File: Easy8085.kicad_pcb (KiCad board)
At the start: 2 copper layers, 37 parts, among them J1 5V Power, J2 EXPANSION, J3 FTDI, SW1 RESET, U1 8085, U2 74LS139, U3 74LS573, U4 CY62256, U5 X28256, U6 8251A, U7 74LS90, Y1 6.144M

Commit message: re-working PCB and schematic to seperate expansion connector and reduce parts.
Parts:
- removed R10, R11, R5, R6, R7, R8, R9: 4.7K, Resistor_THT:R_Axial_DIN0204_L3.6mm_D1.6mm_P7.62mm_Horizontal
- added J4: EXPANSION_B, Connector_PinHeader_2.54mm:PinHeader_1x20_P2.54mm_Vertical, F.Cu at (110.5, 85.1)
- added J5: EXPANSION_D, Connector_PinHeader_2.54mm:PinHeader_1x10_P2.54mm_Vertical, F.Cu at (113.0, 85.1)
- added J6: FTDI, Connector_PinSocket_2.54mm:PinSocket_1x06_P2.54mm_Horizontal, F.Cu at (259.1, 29.4)
- added RN1: 10K, Resistor_THT:R_Array_SIP10, F.Cu at (75.6, 113.0)
- J2: value EXPANSION -> EXPANSION_A; footprint Connector_PinHeader_2.54mm:PinHeader_2x25_P2.54mm_Vertical -> Connector_PinHeader_2.54mm:PinHeader_1x20_P2.54mm_Vertical
- J3: value FTDI -> EXPANSION_C; footprint Connector_PinSocket_2.54mm:PinSocket_1x06_P2.54mm_Horizontal -> Connector_PinHeader_2.54mm:PinHeader_1x10_P2.54mm_Vertical
- U1: footprint Package_DIP:DIP-40_W15.24mm -> Package_DIP:DIP-40_W15.24mm_Socket
- U2: footprint Package_DIP:DIP-16_W7.62mm -> Package_DIP:DIP-16_W7.62mm_Socket
- U3: footprint Package_DIP:DIP-20_W7.62mm -> Package_DIP:DIP-20_W7.62mm_Socket
- U4, U6: footprint Package_DIP:DIP-28_W15.24mm -> Package_DIP:DIP-28_W15.24mm_Socket
- U7: footprint Package_DIP:DIP-14_W7.62mm -> Package_DIP:DIP-14_W7.62mm_Socket
- moved C5 192.4 mm to (262.3, 51.4), turned to 0 degrees
- moved C7 170.9 mm to (198.1, 64.8), turned to 0 degrees
- moved C11 158.3 mm to (251.5, 52.1)
- moved C6 156.0 mm to (193.5, 100.9), turned to 0 degrees
- moved SW1 153.0 mm to (219.3, 66.4)
- moved C8 144.5 mm to (247.0, 61.0)
- moved R3 138.1 mm to (208.2, 66.0), turned to 0 degrees
- moved R4 130.8 mm to (194.6, 93.5), turned to 0 degrees
- moved LED1 125.9 mm to (77.5, 146.7), turned to -90 degrees
- moved C9 124.2 mm to (238.8, 53.3), turned to 0 degrees
- moved R1 113.3 mm to (73.7, 137.8), turned to 180 degrees
- moved C12 113.1 mm to (208.3, 83.8)
- moved J1 112.7 mm to (62.9, 141.0), turned to -90 degrees
- moved R2 111.3 mm to (182.9, 100.7), turned to 0 degrees
- moved C1 111.3 mm to (69.8, 141.6)
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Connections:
- J2 pad 10: /S1 -> /~{INTA}
- J2 pad 11: /RST7.5 -> /AD0
- J2 pad 12: /~{RD} -> /AD1
- J2 pad 13: /RST5.5 -> /AD2
- J2 pad 14: /~{WR} -> /AD3
- J2 pad 15: /INTR -> /AD4
- J2 pad 16: /ALE -> /AD5
- J2 pad 17: /~{INTA} -> /AD6
- J2 pad 18: /S0 -> /AD7
- J2 pad 19: /A0 -> GND
- J2 pad 2: /CLK -> /RES_OUT
- J2 pad 20: /AD0 -> GND
- J2 pad 3: /RES_OUT -> /SOD
- J2 pad 4: /~{RES_IN} -> /SID
- J2 pad 5: /SOD -> /TRAP
- J2 pad 6: /READY -> /RST7.5
- J2 pad 7: /SID -> GND
- J2 pad 8: /IO/~{M} -> /RST5.5
- J2 pad 9: /TRAP -> /INTR
- J3 pad 1: GND -> /ALE
- J3 pad 2: /~{RTS} -> /A0
- J3 pad 3: VCC -> /A1
- J3 pad 4: /RxD -> /A2
- J3 pad 5: /TxD -> /A3
- J3 pad 6: /~{CTS} -> /A4
- R4 pad 1: GND -> VCC
- R4 pad 2: /HOLD -> Net-(R4-Pad2)
- U3 pad 12: /A0 -> /A7
- U3 pad 13: /A1 -> /A6
- U3 pad 14: /A2 -> /A5
- U3 pad 15: /A3 -> /A4
- U3 pad 16: /A4 -> /A3
- U3 pad 17: /A5 -> /A2
- U3 pad 18: /A6 -> /A1
- U3 pad 19: /A7 -> /A0
- U3 pad 2: /AD7 -> /AD0
- U3 pad 3: /AD6 -> /AD1
- U3 pad 4: /AD5 -> /AD2
- U3 pad 5: /AD4 -> /AD3
- U3 pad 6: /AD3 -> /AD4
- U3 pad 7: /AD2 -> /AD5
- U3 pad 8: /AD1 -> /AD6
- U3 pad 9: /AD0 -> /AD7
- U5 pad 27: Net-(R11-Pad2) -> Net-(R4-Pad2)
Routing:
- net /IO/~{M}: track 130.4 -> 0.00 mm
- net /READY: track 86.5 -> 0.00 mm, vias 2 -> 0
- net /~{RES_IN}: track 76.1 -> 0.00 mm
- net /ALE: track 71.5 -> 0.00 mm, vias 2 -> 0
- net /S1: track 63.1 -> 0.00 mm
- net /~{WR}: track 61.8 -> 0.00 mm
- net VCC: track 60.9 -> 0.00 mm
- net /~{RD}: track 60.2 -> 0.00 mm
- net /S0: track 53.6 -> 0.00 mm
- net /RST5.5: track 49.4 -> 0.00 mm
- net /RST7.5: track 48.8 -> 0.00 mm
- net /TRAP: track 46.3 -> 0.00 mm
- net /INTR: track 46.2 -> 0.00 mm
- net /SID: track 44.1 -> 0.00 mm
- net /~{INTA}: track 42.4 -> 0.00 mm
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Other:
- board outline added: 99.1 x 99.1 mm
- copper layers 2 -> 4

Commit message: Continuing PCB layout.
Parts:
- moved J6 203.8 mm to (57.2, 57.7)
- moved SW1 123.9 mm to (95.5, 70.6), turned to 90 degrees
- moved R3 114.5 mm to (95.4, 85.3), turned to -90 degrees
- moved R4 86.8 mm to (125.1, 145.4), turned to 90 degrees
- moved R2 83.0 mm to (100.5, 90.4), turned to 90 degrees
- moved D1 61.1 mm to (97.9, 82.8), turned to -90 degrees
- moved J3 58.1 mm to (55.4, 103.1)
- moved C2 15.0 mm to (100.5, 77.0), turned to 180 degrees
- moved RN1 10.1 mm to (73.2, 103.2)
- moved C1 7.75 mm to (76.2, 137.2)
- moved J5 5.14 mm to (111.3, 80.3)
- moved J2 5.14 mm to (57.9, 80.3)
- moved U3 5.14 mm to (61.7, 103.1)
- moved J4 5.14 mm to (108.7, 80.3)
- moved C3 5.14 mm to (82.6, 72.0)
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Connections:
- J3 pad 1: /ALE -> GND
- J3 pad 10: GND -> /ALE
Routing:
- net /HLDA: track 0.00 -> 73.6 mm
- net /~{INTA}: track 0.00 -> 50.4 mm
- net /INTR: track 0.00 -> 45.9 mm
- net /RST5.5: track 0.00 -> 42.0 mm
- net /HOLD: track 0.00 -> 41.5 mm
- net /A15: track 0.00 -> 40.9 mm
- net /S0: track 0.00 -> 37.6 mm
- net /A14: track 0.00 -> 37.1 mm
- net /A13: track 0.00 -> 33.2 mm
- net /RST7.5: track 0.00 -> 32.9 mm
- net /SID: track 0.00 -> 31.8 mm
- net /A12: track 0.00 -> 29.5 mm
- net /TRAP: track 0.00 -> 28.8 mm
- net /~{WR}: track 0.00 -> 28.7 mm
- net /A11: track 0.00 -> 25.5 mm
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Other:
- outline, holes or cut-outs redrawn

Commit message: Still working on layout - what a pain.
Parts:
- U3: moved to B.Cu
- moved U5 201.1 mm to (-51.7, 103.9)
- moved C3 120.1 mm to (-34.3, 44.8)
- moved C4 120.1 mm to (-29.2, 44.8)
- moved D1 120.1 mm to (-19.1, 55.6)
- moved R2 120.1 mm to (-16.5, 63.2)
- moved R3 120.1 mm to (-21.6, 58.2)
- moved RN1 120.1 mm to (-43.8, 76.1)
- moved U1 120.1 mm to (-39.4, 53.1)
- moved Y1 120.1 mm to (-29.3, 48.6)
- moved U4 116.8 mm to (194.1, 26.4), turned to -90 degrees
- moved C1 102.9 mm to (92.7, 35.6)
- moved J1 102.9 mm to (80.3, 34.3)
- moved R1 102.9 mm to (91.4, 31.8)
- moved LED1 102.1 mm to (82.5, 45.7)
- moved U3 93.0 mm to (-27.9, 78.5), turned to 180 degrees
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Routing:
- net /HLDA: track 73.6 -> 0.00 mm
- net /~{INTA}: track 50.4 -> 0.00 mm
- net /AD7: track 20.7 -> 70.0 mm
- net /AD6: track 20.7 -> 66.3 mm
- net /AD5: track 20.7 -> 62.3 mm
- net /A15: track 40.9 -> 0.00 mm
- net /INTR: track 45.9 -> 6.80 mm
- net /S0: track 37.6 -> 0.00 mm
- net /AD4: track 20.7 -> 58.0 mm
- net /A8: track 15.9 -> 52.3 mm
- net /RST5.5: track 42.0 -> 6.80 mm
- net /AD3: track 20.7 -> 54.9 mm
- net /~{WR}: track 28.7 -> 0.00 mm
- net /RST7.5: track 32.9 -> 6.80 mm
- net /A13: track 33.2 -> 59.0 mm
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
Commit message: Changing to 4 layer board.
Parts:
- U3: moved to F.Cu
- moved RN1 156.8 mm to (106.7, 120.0)
- moved C3 155.7 mm to (115.0, 88.8)
- moved C4 155.7 mm to (120.2, 88.8)
- moved D1 155.7 mm to (130.3, 99.6)
- moved R2 155.7 mm to (132.8, 107.2)
- moved R3 155.7 mm to (127.8, 102.1)
- moved U1 155.7 mm to (110.0, 97.0)
- moved Y1 155.7 mm to (120.1, 92.6)
- moved U4 144.9 mm to (77.5, 112.4), turned to 0 degrees
- moved U3 131.5 mm to (95.9, 122.6), turned to 0 degrees
- moved J1 116.2 mm to (82.5, 150.5), turned to 0 degrees
- moved U5 108.6 mm to (56.6, 112.2), turned to 0 degrees
- moved J6 107.3 mm to (113.1, 149.3), turned to 90 degrees
- moved U2 104.2 mm to (78.7, 107.9)
- moved J3 93.2 mm to (128.3, 45.1)
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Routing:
- net /AD7: track 70.0 -> 0.00 mm
- net /AD6: track 66.3 -> 0.00 mm
- net /AD5: track 62.3 -> 0.00 mm
- net /A13: track 59.0 -> 0.00 mm
- net /AD4: track 58.0 -> 0.00 mm
- net /AD3: track 54.9 -> 0.00 mm
- net /A8: track 52.3 -> 0.00 mm
- net /A14: track 43.2 -> 0.00 mm, vias 1 -> 0
- net /AD2: track 38.3 -> 0.00 mm
- net /A12: track 38.3 -> 0.00 mm
- net /AD1: track 32.9 -> 0.00 mm
- net /AD0: track 25.7 -> 0.00 mm
- net /HOLD: track 25.3 -> 0.00 mm
- net /A5: track 17.0 -> 0.00 mm
- net /A3: track 17.0 -> 0.00 mm
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
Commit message: 4 layer board continued...
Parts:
- removed J4: EXPANSION_B, Connector_PinHeader_2.54mm:PinHeader_1x20_P2.54mm_Vertical
- removed J5: EXPANSION_D, Connector_PinHeader_2.54mm:PinHeader_1x10_P2.54mm_Vertical
- removed J6: FTDI, Connector_PinSocket_2.54mm:PinSocket_1x06_P2.54mm_Horizontal
- J2: value EXPANSION_A -> Expansion; footprint Connector_PinHeader_2.54mm:PinHeader_1x20_P2.54mm_Vertical -> Connector_PinHeader_2.54mm:PinHeader_2x25_P2.54mm_Vertical
- J3: value EXPANSION_C -> FTDI; footprint Connector_PinHeader_2.54mm:PinHeader_1x10_P2.54mm_Vertical -> Connector_PinSocket_2.54mm:PinSocket_1x06_P2.54mm_Horizontal
- moved C9 205.5 mm to (63.5, 160.7)
- moved C8 190.8 mm to (78.7, 150.9)
- moved C5 190.4 mm to (98.4, 148.5), turned to 180 degrees
- moved C11 181.4 mm to (75.1, 94.0), turned to -90 degrees
- moved J2 143.4 mm to (81.3, 156.8), turned to 90 degrees
- moved C7 128.2 mm to (75.7, 102.9), turned to -90 degrees
- moved SW1 123.7 mm to (67.4, 83.9), turned to 0 degrees
- moved C2 85.1 mm to (132.1, 93.3)
- moved R1 77.8 mm to (59.7, 102.7), turned to 0 degrees
- moved C12 69.9 mm to (147.1, 117.5), turned to 90 degrees
- moved C6 68.6 mm to (125.2, 94.3), turned to 90 degrees
- moved C1 62.9 mm to (69.2, 93.9)
- moved LED1 62.7 mm to (56.5, 102.7), turned to 180 degrees
- moved J1 62.0 mm to (62.2, 91.9), turned to -90 degrees
- moved R4 61.7 mm to (60.3, 160.7), turned to 180 degrees
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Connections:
- J2 pad 10: /~{INTA} -> /RST7.5
- J2 pad 11: /AD0 -> /IO/~{M}
- J2 pad 12: /AD1 -> /RST5.5
- J2 pad 13: /AD2 -> /~{RD}
- J2 pad 14: /AD3 -> /INTR
- J2 pad 15: /AD4 -> /~{WR}
- J2 pad 16: /AD5 -> /~{INTA}
- J2 pad 17: /AD6 -> /A15
- J2 pad 18: /AD7 -> /AD0
- J2 pad 19: GND -> /A14
- J2 pad 20: GND -> /A0
- J2 pad 3: /SOD -> /HOLD
- J2 pad 4: /SID -> /SOD
- J2 pad 5: /TRAP -> /HLDA
- J2 pad 6: /RST7.5 -> /SID
- J2 pad 7: GND -> /CLK
- J2 pad 8: /RST5.5 -> /TRAP
- J2 pad 9: /INTR -> /~{RES_IN}
- J3 pad 2: /A0 -> /~{RTS}
- J3 pad 3: /A1 -> VCC
- J3 pad 4: /A2 -> /RxD
- J3 pad 5: /A3 -> /TxD
- J3 pad 6: /A4 -> /~{CTS}
- U3 pad 12: /A7 -> /A0
- U3 pad 13: /A6 -> /A1
- U3 pad 14: /A5 -> /A2
- U3 pad 15: /A4 -> /A3
- U3 pad 16: /A3 -> /A4
- U3 pad 17: /A2 -> /A5
- U3 pad 18: /A1 -> /A6
- U3 pad 19: /A0 -> /A7
- U3 pad 2: /AD0 -> /AD7
- U3 pad 3: /AD1 -> /AD6
- U3 pad 4: /AD2 -> /AD5
- U3 pad 5: /AD3 -> /AD4
- U3 pad 6: /AD4 -> /AD3
- U3 pad 7: /AD5 -> /AD2
- U3 pad 8: /AD6 -> /AD1
- U3 pad 9: /AD7 -> /AD0
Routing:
- net /~{RES_IN}: track 0.00 -> 90.3 mm
- net /AD7: track 0.00 -> 83.5 mm
- net /AD6: track 0.00 -> 79.9 mm
- net /AD5: track 0.00 -> 75.6 mm
- net /AD4: track 0.00 -> 72.1 mm
- net /AD3: track 0.00 -> 68.7 mm
- net /A12: track 0.00 -> 64.9 mm
- net /A1: track 0.00 -> 44.7 mm, vias 0 -> 1
- net /A0: track 0.00 -> 40.9 mm, vias 0 -> 1
- net /ALE: track 0.00 -> 30.3 mm
- net /AD2: track 0.00 -> 29.9 mm
- net /A6: track 0.00 -> 26.0 mm
- net /A7: track 0.00 -> 25.8 mm
- net /AD1: track 0.00 -> 24.4 mm
- net /A14: track 0.00 -> 22.0 mm
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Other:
- board size 99.1 x 99.1 mm -> 99.1 x 81.3 mm

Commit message: Finally making progress on the layout.
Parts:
- added REF**: MountingHole_2.7mm, MountingHole:MountingHole_2.7mm, F.Cu at (89.5, 132.7)
- added REF**: MountingHole_2.7mm, MountingHole:MountingHole_2.7mm, F.Cu at (182.2, 40.0)
- added REF**: MountingHole_2.7mm, MountingHole:MountingHole_2.7mm, F.Cu at (182.2, 132.7)
- added REF**: MountingHole_2.7mm, MountingHole:MountingHole_2.7mm, F.Cu at (89.5, 40.0)
- moved C8 354.5 mm to (413.5, 34.2)
- moved C5 336.4 mm to (413.5, 30.6), turned to 0 degrees
- moved C11 326.6 mm to (398.4, 47.9), turned to 0 degrees
- moved C9 295.8 mm to (351.9, 95.0)
- moved C7 247.7 mm to (323.3, 95.3), turned to 0 degrees
- moved C10 228.9 mm to (372.5, 71.0)
- moved C6 197.0 mm to (321.9, 83.8), turned to 0 degrees
- moved C12 196.1 mm to (341.3, 90.6), turned to 0 degrees
- moved LED1 118.0 mm to (158.1, 42.7), turned to 0 degrees
- moved R1 112.7 mm to (154.9, 42.5), turned to 180 degrees
- moved SW1 112.2 mm to (172.8, 45.4), turned to 180 degrees
- moved J1 111.5 mm to (173.4, 82.6), turned to 90 degrees
- moved J2 99.4 mm to (90.2, 57.8), turned to 0 degrees
- moved C1 99.3 mm to (167.0, 76.7), turned to 90 degrees
- moved U5 98.3 mm to (165.6, 121.2)
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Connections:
- U1 pad 29: /S0 -> unconnected-(U1-Pad29)
- U1 pad 33: /S1 -> unconnected-(U1-Pad33)
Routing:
- net /AD0: track 18.9 -> 141.7 mm, vias 0 -> 2
- net /AD1: track 24.4 -> 137.2 mm, vias 0 -> 2
- net /AD2: track 29.9 -> 132.8 mm, vias 0 -> 2
- net /A5: track 3.81 -> 104.4 mm, vias 0 -> 2
- net /A14: track 22.0 -> 119.4 mm, vias 0 -> 3
- net /A4: track 3.81 -> 100.3 mm, vias 0 -> 2
- net /~{SERIAL}: track 0.00 -> 95.7 mm, vias 0 -> 1
- net /A2: track 3.81 -> 99.0 mm, vias 0 -> 1
- net /A3: track 3.81 -> 97.7 mm, vias 0 -> 2
- net /A7: track 25.8 -> 110.4 mm, vias 0 -> 2
- net /A6: track 26.0 -> 108.5 mm, vias 0 -> 2
- net /A13: track 22.0 -> 93.7 mm, vias 0 -> 2
- net /IO/~{M}: track 0.00 -> 70.6 mm, vias 0 -> 1
- net /A0: track 40.9 -> 103.8 mm
- net /~{CTS}: track 0.00 -> 62.2 mm
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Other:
- board size 99.1 x 81.3 mm -> 99.1 x 99.1 mm
- copper layers 4 -> 2

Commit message: Finish routing the board
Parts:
- moved C8 296.2 mm to (131.3, 124.2), turned to 180 degrees
- moved C10 258.4 mm to (115.0, 50.2)
- moved C5 244.1 mm to (171.6, 62.9), turned to -90 degrees
- moved C7 236.7 mm to (90.0, 55.0), turned to 90 degrees
- moved C11 227.4 mm to (174.8, 89.3)
- moved C6 202.6 mm to (123.7, 41.9)
- moved C12 200.0 mm to (144.7, 126.7), turned to -90 degrees
- moved C9 196.4 mm to (156.8, 71.6), turned to -90 degrees
- moved C2 1.48 mm to (124.0, 49.3)
- moved R2 0.99 mm to (123.6, 63.0)
- moved C3 0.64 mm to (105.5, 43.8)
- moved C4 0.64 mm to (110.5, 43.8)
- moved REF** 0.18 mm to (89.7, 132.6)
- moved REF** 0.18 mm to (182.1, 132.6)
- moved REF** 0.18 mm to (182.1, 40.1)
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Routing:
- net VCC: track 0.00 -> 353.0 mm, vias 0 -> 6
- net /~{RD}: track 49.1 -> 155.3 mm, vias 0 -> 3
- net /~{WR}: track 28.0 -> 127.7 mm, vias 0 -> 2
- net /CLK: track 27.8 -> 94.8 mm, vias 0 -> 1
- net /A11: track 22.4 -> 87.4 mm, vias 0 -> 3
- net /A10: track 22.4 -> 79.5 mm, vias 0 -> 3
- net /RES_OUT: track 7.84 -> 64.6 mm, vias 0 -> 2
- net /A8: track 22.4 -> 77.9 mm, vias 0 -> 2
- net /A9: track 22.4 -> 77.7 mm, vias 0 -> 2
- net /HLDA: track 29.0 -> 77.8 mm, vias 1 -> 4
- net GND: track 0.00 -> 44.3 mm, vias 0 -> 5
- net /RST6.5: track 3.17 -> 46.9 mm, vias 0 -> 1
- net /A0: track 103.8 -> 127.6 mm, vias 1 -> 2
- net /~{ROM}: track 54.0 -> 70.4 mm, vias 0 -> 2
- net /~{RAM}: track 32.4 -> 47.2 mm, vias 0 -> 2
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- added copper zone on B.Cu, net GND

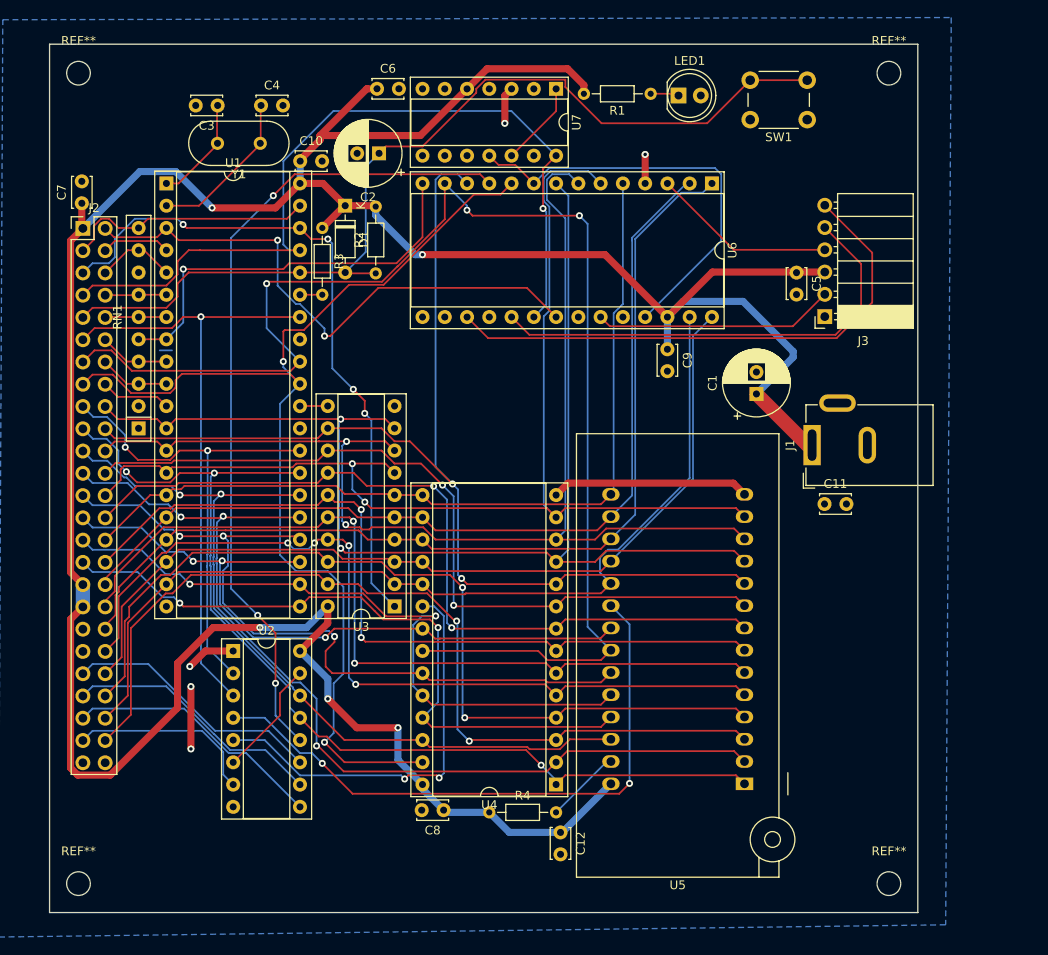
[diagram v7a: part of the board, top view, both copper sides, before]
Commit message: Finished board routing.  Need to fix silkscreen
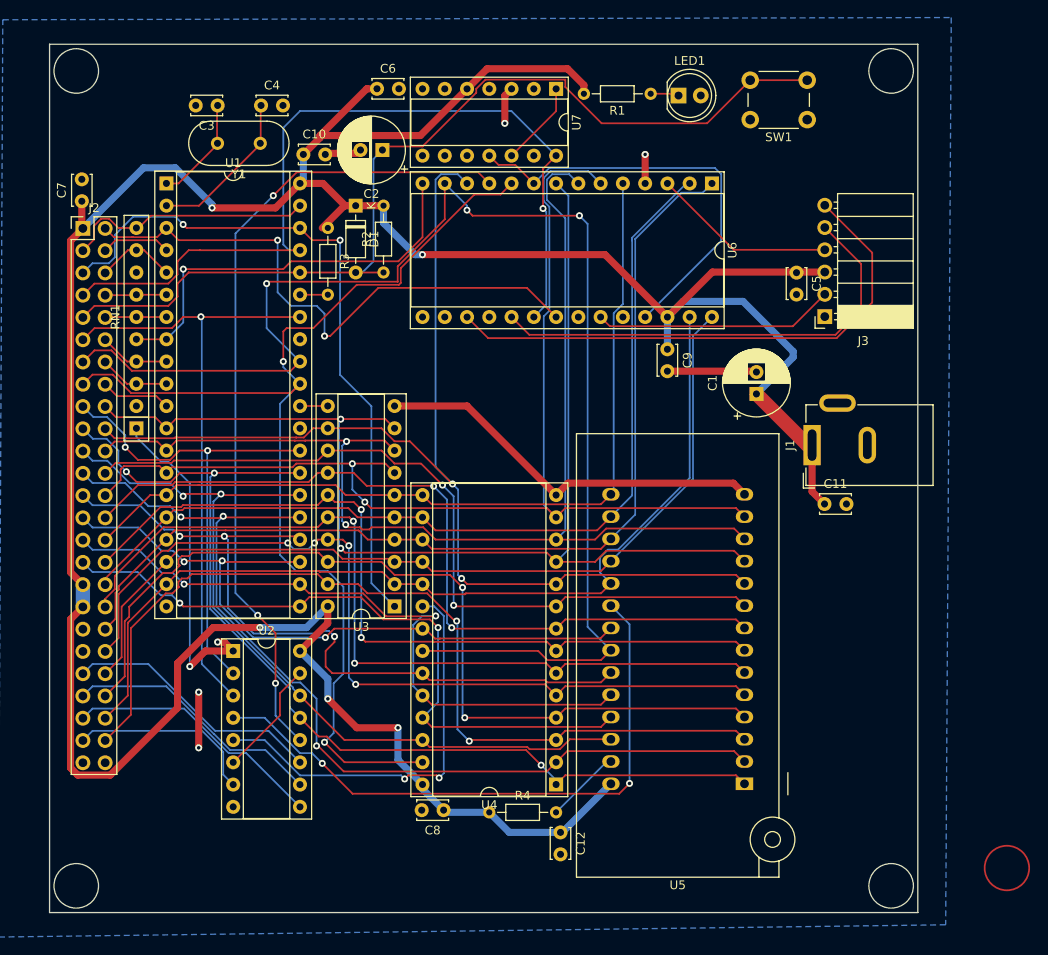
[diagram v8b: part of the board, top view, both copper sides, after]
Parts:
- removed REF** (x4): MountingHole_2.7mm, MountingHole:MountingHole_2.7mm
- moved D1 1.19 mm to (121.3, 55.2)
- moved R2 0.90 mm to (124.5, 62.9)
- moved C10 0.84 mm to (115.3, 49.4)
- moved R3 0.64 mm to (118.1, 57.8)
- moved C2 0.54 mm to (124.3, 48.9)
- moved RN1 0.25 mm to (96.3, 80.6)
- moved C7 0.23 mm to (90.0, 54.7)
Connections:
- U7 pad 13: (no net) -> unconnected-(U7-Pad13)
- U7 pad 4: (no net) -> unconnected-(U7-Pad4)
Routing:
- net GND: track 44.3 -> 111.6 mm, vias 5 -> 6
- net VCC: track 353.0 -> 361.6 mm, vias 6 -> 5
- net /CLK: track 94.8 -> 97.1 mm
- net /RES_OUT: track 64.6 -> 66.0 mm
- net /HLDA: track 77.8 -> 78.9 mm, vias 4 -> 2
- net /~{RD}: track 155.3 -> 156.3 mm
- net /A11: track 87.4 -> 86.6 mm
- net /A6: track 101.3 -> 101.9 mm
- net /A7: track 102.5 -> 103.0 mm
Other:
- outline, holes or cut-outs redrawn
